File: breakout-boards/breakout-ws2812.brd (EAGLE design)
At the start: 20.3 x 14 mm, 7 parts

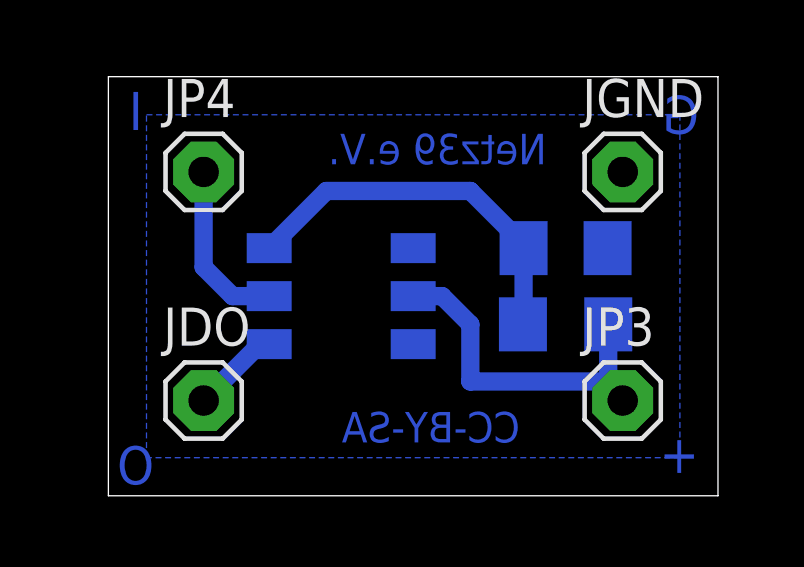
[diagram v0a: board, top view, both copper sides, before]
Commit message: Pin-Raster korrigiert
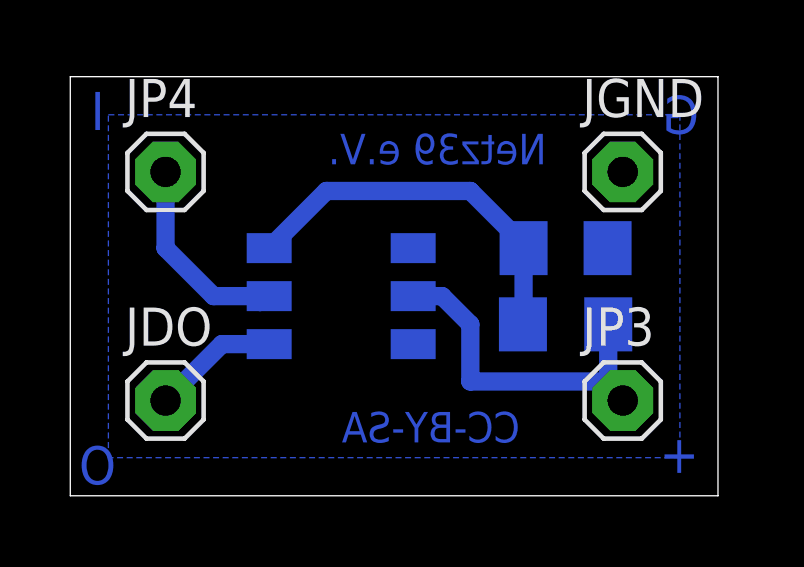
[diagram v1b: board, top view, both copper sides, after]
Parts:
- moved JDO 1.27 mm to (1.91, 3.17)
- moved JP4 1.27 mm to (1.91, 10.8)
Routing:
- net JDI: track 5.76 -> 7.09 mm
- net N$2: track 2.96 -> 4.23 mm
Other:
- board size 20.3 x 14 mm -> 21.6 x 14 mm
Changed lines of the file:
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@@
 <setting verticaltext="up"/>
 </settings>
-<grid distance="0.005" unitdist="inch" unit="inch" style="lines" multiple="1" display="yes" altdistance="0.025" altunitdist="inch" altunit="inch"/>
+<grid distance="0.1" unitdist="inch" unit="inch" style="lines" multiple="1" display="yes" altdistance="0.025" altunitdist="inch" altunit="inch"/>
 <layers>
 <layer number="1" name="Top" color="4" fill="1" visible="yes" active="yes"/>
@@
 <board>
 <plain>
-<wire x1="0" y1="0" x2="20.32" y2="0" width="0" layer="20"/>
+<wire x1="-1.27" y1="0" x2="20.32" y2="0" width="0" layer="20"/>
 <wire x1="20.32" y1="0" x2="20.32" y2="13.97" width="0" layer="20"/>
-<wire x1="20.32" y1="13.97" x2="0" y2="13.97" width="0" layer="20"/>
-<wire x1="0" y1="13.97" x2="0" y2="0" width="0" layer="20"/>
+<wire x1="20.32" y1="13.97" x2="-1.27" y2="13.97" width="0" layer="20"/>
+<wire x1="-1.27" y1="13.97" x2="-1.27" y2="0" width="0" layer="20"/>
 <text x="14.605" y="11.049" size="1.016" layer="16" font="vector" ratio="15" rot="MR0">Netz39 e.V.</text>
 <text x="13.716" y="1.778" size="1.016" layer="16" font="vector" ratio="15" rot="MR0">CC-BY-SA</text>
 <text x="19.685" y="0.762" size="1.27" layer="16" font="vector" rot="MR0">+</text>
 <text x="19.685" y="12.065" size="1.27" layer="16" font="vector" rot="MR0">G</text>
-<text x="1.524" y="0.381" size="1.27" layer="16" font="vector" rot="MR0">O</text>
-<text x="1.143" y="12.192" size="1.27" layer="16" font="vector" rot="MR0">I</text>
+<text x="0.254" y="0.381" size="1.27" layer="16" font="vector" rot="MR0">O</text>
+<text x="-0.127" y="12.192" size="1.27" layer="16" font="vector" rot="MR0">I</text>
 </plain>
 <attributes>
@@
 <element name="C1" library="resistor" package="C1206" value="" x="15.24" y="8.255" rot="MR180"/>
 <element name="JP3" library="pinhead" package="1X01" value="VDD" x="17.145" y="3.175"/>
-<element name="JP4" library="pinhead" package="1X01" value="DI" x="3.175" y="10.795"/>
+<element name="JP4" library="pinhead" package="1X01" value="DI" x="1.905" y="10.795"/>
 <element name="JGND" library="pinhead" package="1X01" value="GND" x="17.145" y="10.795"/>
-<element name="JDO" library="pinhead" package="1X01" value="DO" x="3.175" y="3.175"/>
+<element name="JDO" library="pinhead" package="1X01" value="DO" x="1.905" y="3.175"/>
 </elements>
 <signals>
 <signal name="GND">
 <polygon width="0.4064" layer="16">
-<vertex x="1.27" y="12.7"/>
+<vertex x="0" y="12.7"/>
 <vertex x="19.05" y="12.7"/>
 <vertex x="19.05" y="1.27"/>
-<vertex x="1.27" y="1.27"/>
+<vertex x="0" y="1.27"/>
 </polygon>
 <contactref element="C1" pad="2"/>
@@
 <contactref element="U$1" pad="2"/>
 <contactref element="JP4" pad="1"/>
-<wire x1="3.175" y1="10.795" x2="3.175" y2="7.62" width="0.6096" layer="16"/>
-<wire x1="4.14" y1="6.655" x2="5.36" y2="6.655" width="0.6096" layer="16"/>
-<wire x1="3.175" y1="7.62" x2="4.14" y2="6.655" width="0.6096" layer="16"/>
+<wire x1="5.36" y1="6.655" x2="5.055" y2="6.35" width="0.4064" layer="16"/>
+<wire x1="1.905" y1="8.255" x2="1.905" y2="10.795" width="0.6096" layer="16"/>
+<wire x1="1.905" y1="8.255" x2="3.505" y2="6.655" width="0.6096" layer="16"/>
+<wire x1="3.505" y1="6.655" x2="5.36" y2="6.655" width="0.6096" layer="16"/>
 </signal>
 <signal name="N$2">
 <contactref element="U$1" pad="1"/>
 <contactref element="JDO" pad="1"/>
-<wire x1="3.175" y1="3.175" x2="5.055" y2="5.055" width="0.6096" layer="16"/>
-<wire x1="5.055" y1="5.055" x2="5.36" y2="5.055" width="0.4064" layer="16"/>
+<wire x1="1.905" y1="3.175" x2="3.785" y2="5.055" width="0.6096" layer="16"/>
+<wire x1="3.785" y1="5.055" x2="5.36" y2="5.055" width="0.6096" layer="16"/>
 </signal>
 </signals>
